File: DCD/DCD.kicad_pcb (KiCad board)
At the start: 4 copper layers, 110 x 110 mm, 117 parts, among them J1 UMPS-04-03.5-G-VT-SM-WT, J2 UMPS-04-03.5-G-VT-SM-WT, J3 UMPS-04-03.5-G-VT-SM-WT, J4 UMPS-04-03.5-G-VT-SM-WT, U1 LP2985-18DBVR, U10 DAC8811ICDGKT, U11 OPA277UA, U12 OPA277UA, U2 LP2985-50DBVR, U3 LP2985-33DBVR, U4 ADR4550BRZ, U5 ADA4945-1ACPZ-R2, U6 ADA4945-1ACPZ-R2, U7 AD4630-24BBCZ, U8 OPA277UA, U9 DAC8811ICDGKT

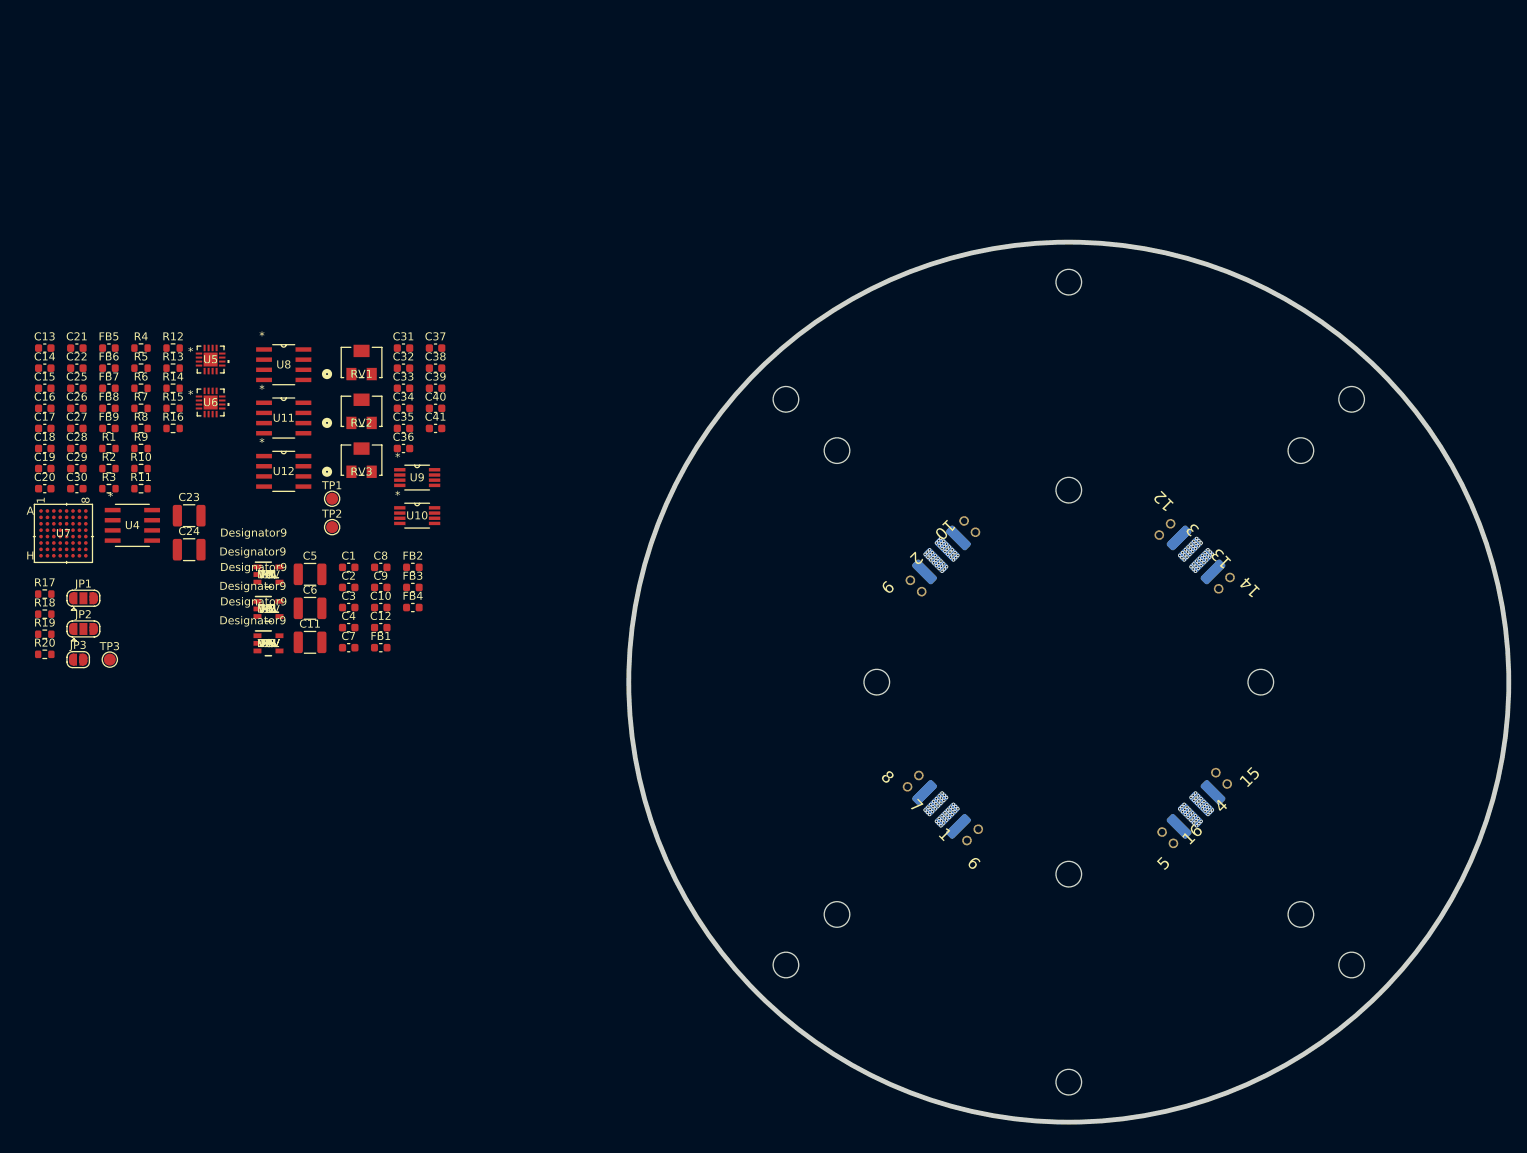
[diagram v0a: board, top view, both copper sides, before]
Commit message: Finished
Final touches, PSUs filtering, external connections, psu connections for
the negative voltage, and the DAC higher voltage, and the negative
voltage. Added an external connection directely to the DAC.
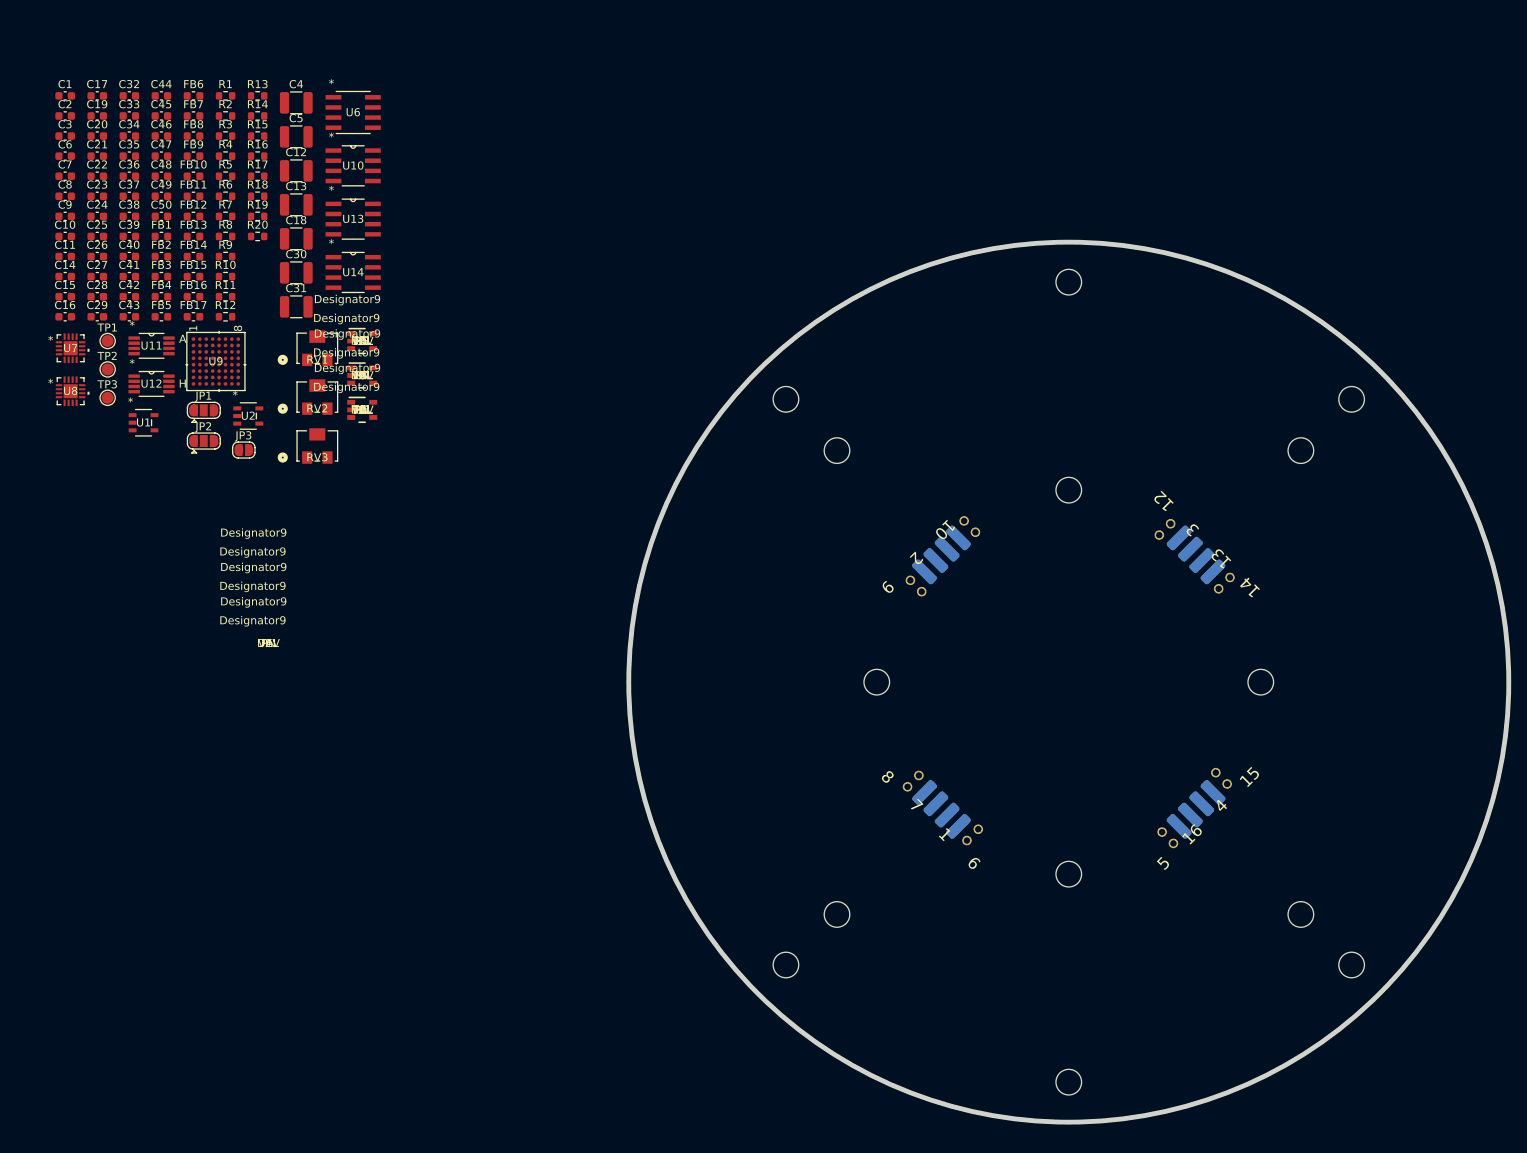
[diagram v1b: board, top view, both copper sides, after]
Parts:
- added C42: 1nF, Capacitor_SMD:C_0603_1608Metric, F.Cu at (29.3, 46.9)
- added C43: 1nF, Capacitor_SMD:C_0603_1608Metric, F.Cu at (29.3, 49.4)
- added C44: 10pF, Capacitor_SMD:C_0603_1608Metric, F.Cu at (33.3, 21.8)
- added C45: 10pF, Capacitor_SMD:C_0603_1608Metric, F.Cu at (33.3, 24.3)
- added C46: 100nF, Capacitor_SMD:C_0603_1608Metric, F.Cu at (33.3, 26.8)
- added C47: 100nF, Capacitor_SMD:C_0603_1608Metric, F.Cu at (33.3, 29.3)
- added C48: 100nF, Capacitor_SMD:C_0603_1608Metric, F.Cu at (33.3, 31.8)
- added C49: 100nF, Capacitor_SMD:C_0603_1608Metric, F.Cu at (33.3, 34.3)
- added C50: 100nF, Capacitor_SMD:C_0603_1608Metric, F.Cu at (33.3, 36.9)
- added FB10: 470Ω, Inductor_SMD:L_0603_1608Metric, F.Cu at (37.3, 31.8)
- added FB11: 470Ω, Inductor_SMD:L_0603_1608Metric, F.Cu at (37.3, 34.3)
- added FB12: 470Ω, Inductor_SMD:L_0603_1608Metric, F.Cu at (37.3, 36.9)
- added FB13: 470Ω, Inductor_SMD:L_0603_1608Metric, F.Cu at (37.3, 39.4)
- added FB14: 470Ω, Inductor_SMD:L_0603_1608Metric, F.Cu at (37.3, 41.9)
- added FB15: 470Ω, Inductor_SMD:L_0603_1608Metric, F.Cu at (37.3, 44.4)
- added FB16: 470Ω, Inductor_SMD:L_0603_1608Metric, F.Cu at (37.3, 46.9)
- added FB17: 470Ω, Inductor_SMD:L_0603_1608Metric, F.Cu at (37.3, 49.4)
- added U13: OPA277UA, custom_components:D8, F.Cu at (57.3, 37.2)
- added U14: OPA277UA, custom_components:D8, F.Cu at (57.3, 43.9)
- C11: value 10uF -> 10nF; footprint Capacitor_SMD:C_1210_3225Metric -> Capacitor_SMD:C_0603_1608Metric
- C12: value 100nF -> 10uF; footprint Capacitor_SMD:C_0603_1608Metric -> Capacitor_SMD:C_1210_3225Metric
- C13: value 100p -> 10uF; footprint Capacitor_SMD:C_0603_1608Metric -> Capacitor_SMD:C_1210_3225Metric
- C14, C15, C19, C33: value 100p -> 100nF
- C16: value 100p -> 1µF
- C17: value 1µF -> 10nF
- C18, C30: value 1nF -> 10uF; footprint Capacitor_SMD:C_0603_1608Metric -> Capacitor_SMD:C_1210_3225Metric
- C20: value 1µF -> 100p
- C21, C22, C26, C40, C41: value 100nF -> 100p
- C23: value 10uF -> 100p; footprint Capacitor_SMD:C_1210_3225Metric -> Capacitor_SMD:C_0603_1608Metric
- C24: value 10uF -> 1µF; footprint Capacitor_SMD:C_1210_3225Metric -> Capacitor_SMD:C_0603_1608Metric
- C25: value 100nF -> 1nF
- C27: value 1nF -> 1µF
- C28, C29: value 1nF -> 100nF
- C3: value 10nF -> 1µF
- C31: value 1µF -> 10uF; footprint Capacitor_SMD:C_0603_1608Metric -> Capacitor_SMD:C_1210_3225Metric
- C32: value 1µF -> 100nF
- C34: value 100p -> 1nF
- C37: value 10pF -> 1nF
- C38: value 10pF -> 1µF
- C39, C7: value 100nF -> 1µF
- C4: value 10nF -> 10uF; footprint Capacitor_SMD:C_0603_1608Metric -> Capacitor_SMD:C_1210_3225Metric
- C6: value 10uF -> 100nF; footprint Capacitor_SMD:C_1210_3225Metric -> Capacitor_SMD:C_0603_1608Metric
- U1: value LP2985-18DBVR -> TLV76780DBVR; footprint custom_components:DBV0005A_N -> custom_components:SOT_80DBVR_TEX
- U10: value DAC8811ICDGKT -> OPA277UA; footprint custom_components:DGK8 -> custom_components:D8
- U11, U12: value OPA277UA -> DAC8811ICDGKT; footprint custom_components:D8 -> custom_components:DGK8
- U2: value LP2985-50DBVR -> ADP7182AUJZ-1.8-R7; footprint custom_components:DBV0005A_N -> custom_components:UJ-5_ADI
- U3: value LP2985-33DBVR -> LP2985-50DBVR
- U4: value ADR4550BRZ -> LP2985-18DBVR; footprint custom_components:R_8_ADI -> custom_components:DBV0005A_N
- U5: value ADA4945-1ACPZ-R2 -> LP2985-33DBVR; footprint custom_components:LFCSP16_ADA4945-1ACPZ-R2_ADI -> custom_components:DBV0005A_N
- U6: value ADA4945-1ACPZ-R2 -> ADR4550BRZ; footprint custom_components:LFCSP16_ADA4945-1ACPZ-R2_ADI -> custom_components:R_8_ADI
- U7: value AD4630-24BBCZ -> ADA4945-1ACPZ-R2; footprint custom_components:05-08-1797_ADI -> custom_components:LFCSP16_ADA4945-1ACPZ-R2_ADI
- U8: value OPA277UA -> ADA4945-1ACPZ-R2; footprint custom_components:D8 -> custom_components:LFCSP16_ADA4945-1ACPZ-R2_ADI
- U9: value DAC8811ICDGKT -> AD4630-24BBCZ; footprint custom_components:DGK8 -> custom_components:05-08-1797_ADI
- moved C1 68.8 mm to (21.3, 21.8)
- moved C3 68.8 mm to (21.3, 26.8)
- moved C2 68.8 mm to (21.3, 24.3)
- moved C7 68.8 mm to (21.3, 31.8)
- moved C4 65.9 mm to (50.1, 22.7)
- moved C6 64.3 mm to (21.3, 29.3)
- moved C10 60.9 mm to (21.3, 39.4)
- moved C8 60.9 mm to (21.3, 34.3)
- moved C9 60.9 mm to (21.3, 36.9)
- moved R17 58.6 mm to (45.3, 31.8)
- moved R18 58.6 mm to (45.3, 34.3)
- moved R19 58.6 mm to (45.3, 36.9)
- moved R20 58.6 mm to (45.3, 39.4)
- moved FB1 58.3 mm to (33.3, 39.4)
- moved C12 58.1 mm to (50.1, 31.2)
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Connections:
- C1 pad 1: /Comms/Vin -> /Comms/+Vin
- C11 pad 1: Net-(U3-VOUT) -> /ADC/GND
- C11 pad 2: /ADC/GND -> Net-(U4-BYPASS)
- C13 pad 1: /ADC/IN0 -> Net-(U4-VOUT)
- C13 pad 2: Net-(U5--FB) -> /ADC/GND
- C14 pad 1: Net-(U5--IN) -> Net-(U3-VOUT)
- C14 pad 2: Net-(U5-+FB) -> /ADC/GND
- C15 pad 1: /ADC/IN1 -> Net-(U4-VOUT)
- C15 pad 2: Net-(U6--FB) -> /ADC/GND
- C16 pad 1: Net-(U6--IN) -> Net-(U3-VOUT)
- C16 pad 2: Net-(U6-+FB) -> /ADC/GND
- C17 pad 1: Net-(U5-Vocm) -> /ADC/GND
- C17 pad 2: /ADC/GND -> Net-(U5-BYPASS)
- C18 pad 1: Net-(U5-Vocm) -> Net-(U5-VOUT)
- C19 pad 1: Net-(U5-Vocm) -> Net-(U5-VOUT)
- C2 pad 1: /Comms/Vin -> /Comms/-Vin
- C20 pad 1: /ADC/5V -> /ADC/IN0
- C20 pad 2: /ADC/GND -> Net-(U7--FB)
- C21 pad 1: /ADC/5V -> Net-(U7--IN)
- C21 pad 2: /ADC/GND -> Net-(U7-+FB)
- C22 pad 1: Net-(U4-VOUT) -> /ADC/IN1
- C22 pad 2: /ADC/GND -> Net-(U8--FB)
- C23 pad 1: Net-(U7-REFIN) -> Net-(U8--IN)
- C23 pad 2: /ADC/GND -> Net-(U8-+FB)
- C24 pad 1: /ADC/VRef -> Net-(U7-Vocm)
- C25 pad 1: Net-(U7-REFIN) -> Net-(U7-Vocm)
- C26 pad 1: /ADC/VRef -> Net-(U7-Vocm)
- C27 pad 1: Net-(U7-IN0+) -> /ADC/7V
- C28 pad 1: Net-(U7-IN1+) -> /ADC/7V
- C29 pad 1: Net-(U7-IN0-) -> Net-(U6-VOUT)
- C3 pad 1: /ADC/GND -> /Comms/-Vin
- C3 pad 2: Net-(U1-BYPASS) -> /ADC/GND
- C30 pad 1: Net-(U7-IN1-) -> Net-(U9-REFIN)
- C31 pad 1: /DAC/3.3V -> /ADC/VRef
- C32 pad 1: /DAC/3.3V -> Net-(U9-REFIN)
- C33 pad 1: /DAC/3.3V -> /ADC/VRef
- C34 pad 1: /DAC/3.3V -> Net-(U9-IN0+)
- C35 pad 1: /DAC/3.3V -> Net-(U9-IN1+)
- C36 pad 1: /DAC/3.3V -> Net-(U9-IN0-)
- C37 pad 1: /DAC/DAC0 -> Net-(U9-IN1-)
- C37 pad 2: Net-(U9-IOUT) -> /ADC/GND
- C38 pad 1: /DAC/DAC1 -> /DAC/3.3V
- C38 pad 2: Net-(U10-IOUT) -> /ADC/GND
- C39 pad 1: /ADC/VRef -> /DAC/3.3V
- C4 pad 1: /ADC/GND -> Net-(U1-OUT)
- C4 pad 2: Net-(U2-BYPASS) -> /ADC/GND
- C40 pad 1: /Comms/VRef -> /DAC/3.3V
- C41 pad 1: /Comms/VRef -> /DAC/3.3V
- C5 pad 1: Net-(U1-VOUT) -> Net-(U2-VOUT)
- C6 pad 1: Net-(U2-VOUT) -> Net-(U1-OUT)
- C7 pad 1: Net-(U1-VOUT) -> Net-(U1-OUT)
- C9 pad 1: Net-(U2-VOUT) -> Net-(U1-OUT)
- FB1 pad 1: Net-(U1-VOUT) -> Net-(U1-OUT)
- FB1 pad 2: /ADC/VIO -> /ADC/7V
- FB2 pad 2: /ADC/5V -> /DAC/-1.2V
- FB3 pad 1: Net-(U1-VOUT) -> Net-(U3-VOUT)
- FB3 pad 2: /ADC/1.8V -> /ADC/5V
- FB4 pad 1: Net-(U3-VOUT) -> Net-(U4-VOUT)
- FB4 pad 2: /DAC/3.3V -> /ADC/VIO
- FB5 pad 2: Net-(FB5-Pad2) -> /ADC/1.8V
- FB6 pad 1: Net-(U4-VOUT) -> Net-(U5-VOUT)
- FB6 pad 2: Net-(FB6-Pad2) -> /DAC/3.3V
- FB7 pad 1: /ADC/SDO1 -> Net-(U6-VOUT)
- FB7 pad 2: Net-(U7-SDO1) -> Net-(FB7-Pad2)
- FB8 pad 1: /ADC/SDO0 -> Net-(U6-VOUT)
- FB8 pad 2: Net-(U7-SDO0) -> Net-(FB8-Pad2)
- FB9 pad 1: /ADC/BSY -> /ADC/SDO0
- FB9 pad 2: Net-(U7-BUSY/SCKOUT) -> Net-(U9-SDO0)
- J1 pad 2: /ADC/SDO1 -> /ADC/~{CS}
- J1 pad 3: (no net) -> Net-(J1-Pin_3)
- J1 pad 4: (no net) -> Net-(J1-Pin_4)
- J2 pad 1: (no net) -> Net-(J2-Pin_1)
- J2 pad 2: (no net) -> Net-(J2-Pin_2)
- J2 pad 3: /ADC/BSY -> /ADC/CNV
- J2 pad 4: (no net) -> /Comms/*CS
- J3 pad 1: (no net) -> Net-(J3-Pin_1)
- J3 pad 2: (no net) -> /ADC/BSY
- J3 pad 3: (no net) -> Net-(J3-Pin_3)
- J3 pad 4: (no net) -> Net-(J3-Pin_4)
- J4 pad 1: /Comms/Vin -> /Comms/VRef
- J4 pad 2: /Comms/VRef -> /ADC/GND
- J4 pad 3: /ADC/GND -> /Comms/DAC_Ext
- J4 pad 4: (no net) -> /Comms/Ext
- R1 pad 2: Net-(U5--FB) -> Net-(U7--FB)
- R10 pad 1: Net-(FB5-Pad2) -> Net-(FB7-Pad2)
- R10 pad 2: Net-(U7-REFIN) -> Net-(U9-REFIN)
- R11 pad 1: Net-(FB6-Pad2) -> Net-(FB8-Pad2)
- R12 pad 1: Net-(U5-+OUT) -> Net-(U7-+OUT)
- R12 pad 2: Net-(U7-IN0+) -> Net-(U9-IN0+)
- R13 pad 1: Net-(U6-+OUT) -> Net-(U8-+OUT)
- R13 pad 2: Net-(U7-IN1+) -> Net-(U9-IN1+)
- R14 pad 1: Net-(U5--OUT) -> Net-(U7--OUT)
- R14 pad 2: Net-(U7-IN0-) -> Net-(U9-IN0-)
- R15 pad 1: Net-(U6--OUT) -> Net-(U8--OUT)
- R15 pad 2: Net-(U7-IN1-) -> Net-(U9-IN1-)
- R16 pad 2: Net-(U7-*RST) -> Net-(U9-*RST)
- R19 pad 2: /DAC/DAC0 -> /Comms/DAC_Ext
- R2 pad 1: Net-(U5-+FB) -> Net-(U7-+FB)
- R2 pad 2: Net-(U5--IN) -> Net-(U7--IN)
- R3 pad 2: Net-(U5--IN) -> Net-(U7--IN)
- R4 pad 2: Net-(U6--FB) -> Net-(U8--FB)
- R5 pad 1: Net-(U6-+FB) -> Net-(U8-+FB)
- R5 pad 2: Net-(U6--IN) -> Net-(U8--IN)
- R6 pad 2: Net-(U6--IN) -> Net-(U8--IN)
- R7 pad 1: Net-(U5-Vocm) -> Net-(U7-Vocm)
- R8 pad 2: Net-(U5-Vocm) -> Net-(U7-Vocm)
- R9 pad 1: Net-(U5-MODE) -> Net-(U7-MODE)
- RV1 pad 2: /ADC/VRef -> /ADC/7V
- RV2 pad 2: /Comms/VRef -> /ADC/7V
- RV3 pad 2: /Comms/VRef -> /ADC/7V
- TP1 pad 1: /DAC/DAC0 -> /Comms/DAC_Ext
- U1 pad 1: /Comms/Vin -> /Comms/+Vin
- U1 pad 3: /Comms/Vin -> /Comms/+Vin
- U1 pad 4: Net-(U1-BYPASS) -> unconnected-(U1-DNC-Pad4)
- U1 pad 5: Net-(U1-VOUT) -> Net-(U1-OUT)
- U10 pad 1: /Comms/CLK -> Net-(RV1-Pad3)
- U10 pad 2: /Comms/SDI2 -> /Comms/VRef
- U10 pad 3: /DAC/DAC1 -> /ADC/VRef
- U10 pad 4: /Comms/VRef -> /ADC/GND
- U10 pad 5: Net-(U10-IOUT) -> unconnected-(U10-NC-Pad5)
- U10 pad 6: /ADC/GND -> /Comms/VRef
- U10 pad 7: /DAC/3.3V -> /ADC/7V
- U10 pad 8: /Comms/*CS2 -> Net-(RV1-Pad1)
- U11 pad 1: Net-(RV2-Pad3) -> /Comms/CLK
- U11 pad 2: Net-(U9-IOUT) -> /Comms/SDI1
- U11 pad 3: /ADC/GND -> /Comms/DAC_Ext
- U11 pad 4: /ADC/GND -> /Comms/VRef
- U11 pad 5: unconnected-(U11-NC-Pad5) -> Net-(U11-IOUT)
- U11 pad 6: /DAC/DAC0 -> /ADC/GND
- U11 pad 7: /Comms/VRef -> /DAC/3.3V
- U11 pad 8: Net-(RV2-Pad1) -> /Comms/*CS
- U12 pad 1: Net-(RV3-Pad3) -> /Comms/CLK
- U12 pad 2: Net-(U10-IOUT) -> /Comms/SDI2
- U12 pad 3: /ADC/GND -> /DAC/DAC1
- U12 pad 4: /ADC/GND -> /Comms/VRef
- U12 pad 5: unconnected-(U12-NC-Pad5) -> Net-(U12-IOUT)
- U12 pad 6: /DAC/DAC1 -> /ADC/GND
- U12 pad 7: /Comms/VRef -> /DAC/3.3V
- U12 pad 8: Net-(RV3-Pad1) -> /Comms/*CS
- U2 pad 1: /Comms/Vin -> /ADC/GND
- U2 pad 2: /ADC/GND -> /Comms/-Vin
- U2 pad 3: /Comms/Vin -> /Comms/-Vin
- U2 pad 4: Net-(U2-BYPASS) -> unconnected-(U2-NC-Pad4)
- U3 pad 1: Net-(U2-VOUT) -> Net-(U1-OUT)
- U3 pad 3: Net-(U2-VOUT) -> Net-(U1-OUT)
- U4 pad 1: unconnected-(U4-NC-Pad1) -> Net-(U1-OUT)
- U4 pad 2: /ADC/5V -> /ADC/GND
- U4 pad 3: unconnected-(U4-NC-Pad3) -> Net-(U1-OUT)
- U4 pad 4: /ADC/GND -> Net-(U4-BYPASS)
- U4 pad 5: unconnected-(U4-NC-Pad5) -> Net-(U4-VOUT)
- U5 pad 1: Net-(U5--FB) -> Net-(U3-VOUT)
- U5 pad 2: /ADC/IN0 -> /ADC/GND
- U5 pad 3: Net-(U5--IN) -> Net-(U3-VOUT)
- U5 pad 4: Net-(U5-+FB) -> Net-(U5-BYPASS)
- U5 pad 5: Net-(U5-MODE) -> Net-(U5-VOUT)
- U6 pad 1: Net-(U6--FB) -> unconnected-(U6-NC-Pad1)
- U6 pad 2: /ADC/IN1 -> /ADC/7V
- U6 pad 3: Net-(U6--IN) -> unconnected-(U6-NC-Pad3)
- U6 pad 4: Net-(U6-+FB) -> /ADC/GND
- U6 pad 5: Net-(U5-MODE) -> unconnected-(U6-NC-Pad5)
- U6 pad 6: /ADC/5V -> Net-(U6-VOUT)
- U6 pad 7: /ADC/5V -> unconnected-(U6-NC-Pad7)
- U6 pad 8: /ADC/5V -> unconnected-(U6-TP-Pad8)
- U8 pad 1: Net-(RV1-Pad3) -> Net-(U8--FB)
- U8 pad 2: /Comms/VRef -> /ADC/IN1
- U8 pad 3: /ADC/VRef -> Net-(U8--IN)
- U8 pad 4: /ADC/GND -> Net-(U8-+FB)
- U8 pad 5: unconnected-(U8-NC-Pad5) -> Net-(U7-MODE)
- U8 pad 6: /Comms/VRef -> /ADC/5V
- U8 pad 7: /ADC/VRef -> /ADC/5V
- U8 pad 8: Net-(RV1-Pad1) -> /ADC/5V
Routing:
- net /Comms/VRef: vias 21 -> 0
- net /Comms/SDI2: vias 21 -> 0
- net /Comms/*CS1: vias 21 -> 0
- net /ADC/~{CS}: vias 21 -> 0
- net /ADC/SDO1: vias 21 -> 0
- net /ADC/GND: vias 21 -> 0
- net /ADC/CNV: vias 21 -> 0
- net /ADC/BSY: vias 21 -> 0

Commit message: Progress on the component placement
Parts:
- removed JP3: SolderJumper_2_Open, Jumper:SolderJumper-2_P1.3mm_Open_RoundedPad1.0x1.5mm
- added C51: 10uF, Capacitor_SMD:C_1210_3225Metric, F.Cu at (73.5, 40.2)
- added C52: 10uF, Capacitor_SMD:C_1210_3225Metric, F.Cu at (101.6, 43.0)
- added C53: 10uF, Capacitor_SMD:C_1210_3225Metric, F.Cu at (148.2, 22.3)
- added C54: 10uF, Capacitor_SMD:C_1210_3225Metric, F.Cu at (112.6, 29.7)
- added C55: 10uF, Capacitor_SMD:C_1210_3225Metric, F.Cu at (148.2, 26.5)
- added C56: 10uF, Capacitor_SMD:C_1210_3225Metric, F.Cu at (96.8, 20.0)
- moved C15 133.3 mm to (153.0, 26.5)
- moved C11 133.0 mm to (153.0, 24.0)
- moved C9 132.7 mm to (153.0, 21.4)
- moved FB4 121.1 mm to (153.0, 29.0)
- moved FB5 121.1 mm to (153.0, 31.5)
- moved C46 120.7 mm to (76.7, 139.4)
- moved C44 120.7 mm to (76.7, 134.4)
- moved C45 120.7 mm to (76.7, 136.9)
- moved C47 120.7 mm to (76.7, 141.9)
- moved C48 110.7 mm to (80.7, 131.9)
- moved C50 110.7 mm to (80.7, 136.9)
- moved C49 110.7 mm to (80.7, 134.4)
- moved TP2 106.8 mm to (79.9, 148.5)
- moved TP1 106.8 mm to (79.9, 145.0)
- moved C40 104.5 mm to (72.7, 136.9)
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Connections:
- FB2 pad 2: /DAC/-1.2V -> /PSUs/-1.8V
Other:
- board text removed: "DEV"
- board text removed: "Designator9"
- board text removed: "PN"
- board text removed: "VAL"

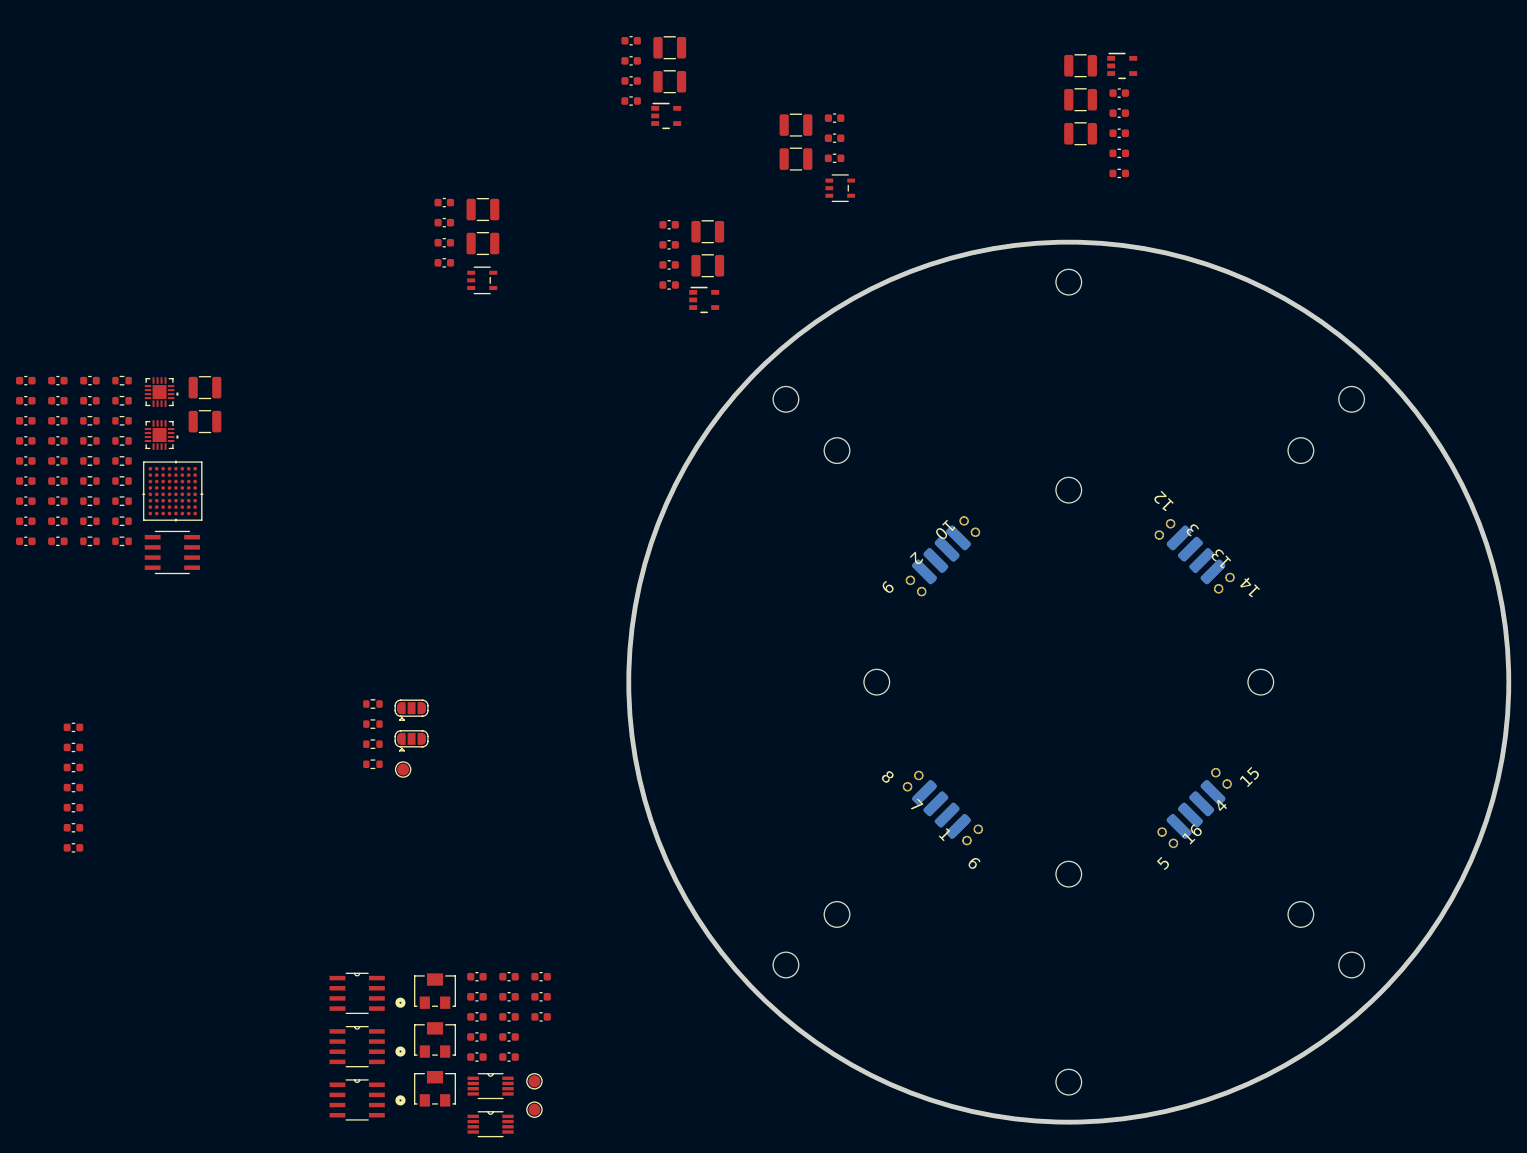
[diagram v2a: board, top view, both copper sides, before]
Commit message: Progress on fixing the remaining footprints and 3 models
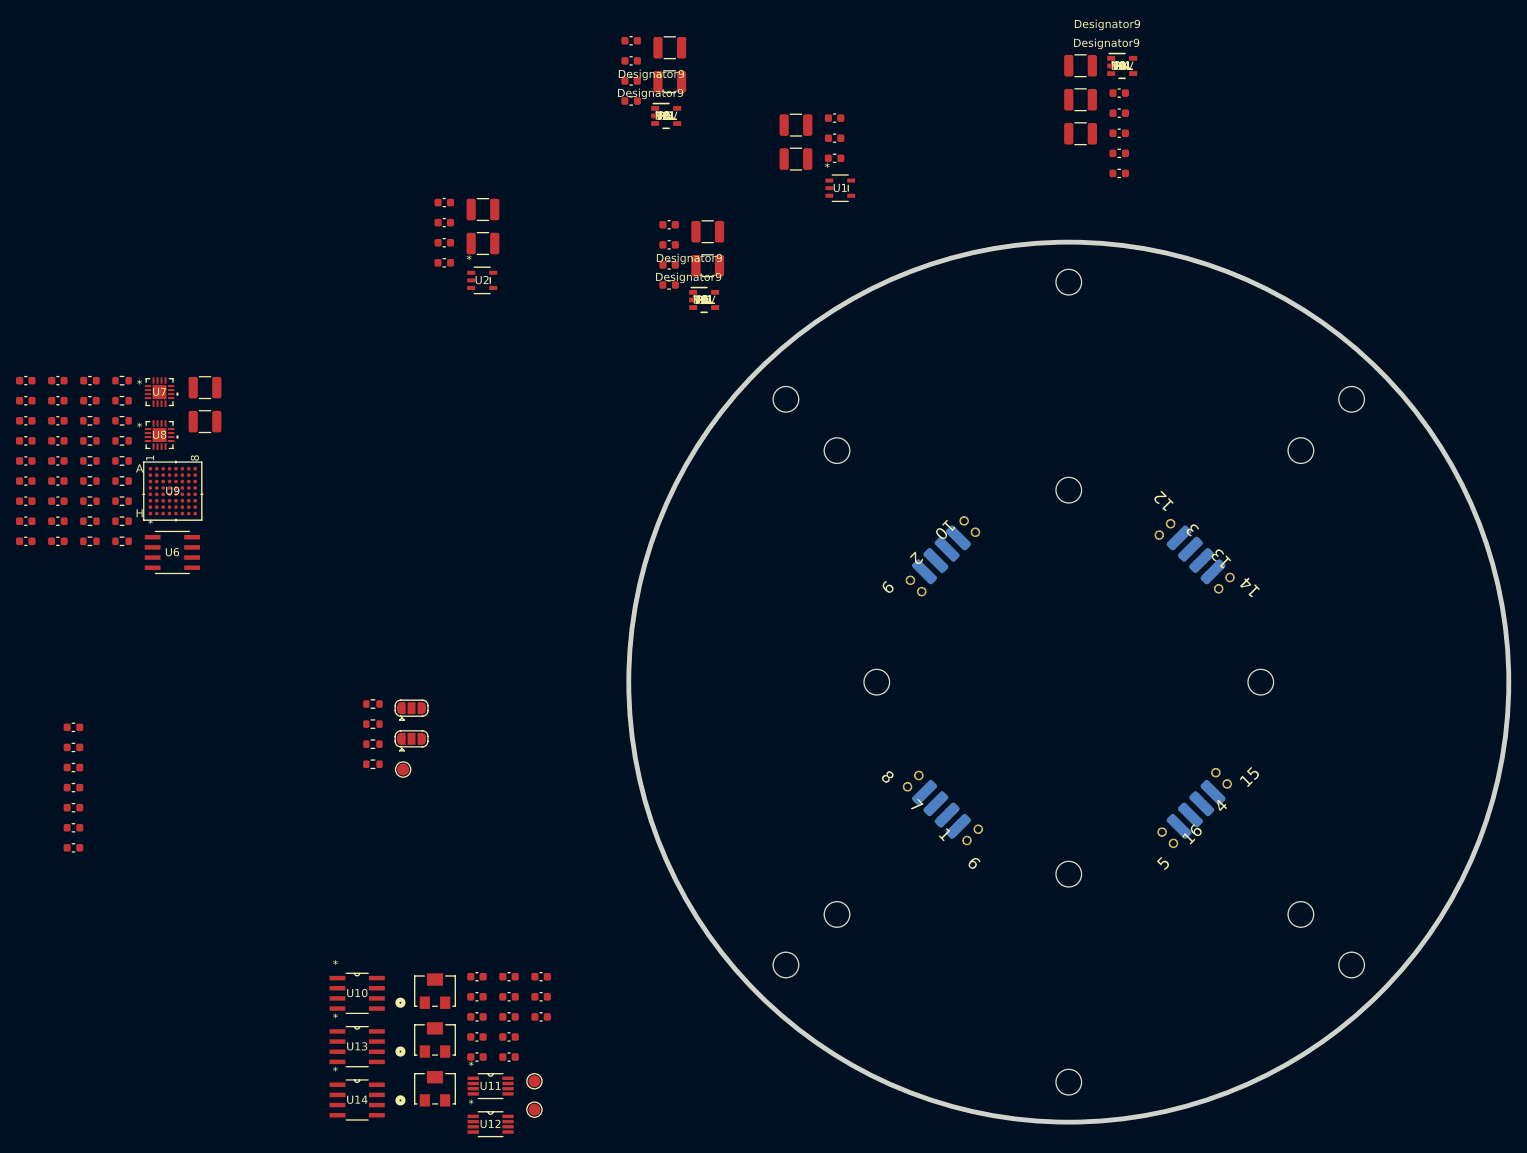
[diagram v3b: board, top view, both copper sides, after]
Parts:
- H15: value Threaded spacer M3x5mm -> Spacer M3x5mm
- J1, J2, J3, J4: footprint LOBSTER:UMPS-04-03.5-G-VT-SM-WT -> custom_components:UMPS-04-03.5-G-VT-SM-WT
